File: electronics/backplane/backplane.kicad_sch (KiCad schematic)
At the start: 22 parts, among them J1 USB_C_SOCKET_RA_PTH_SIMPLE, P1 JST_SH_4_RA, P2 JST_SH_4_RA, P3 JST_SH_4_RA, P4 JST_SH_4_RA, P5 PAD_SOLDER_2mm, SW1 B3U-1000P_SPST-NO_SMD, SW2 B3U-1000P_SPST-NO_SMD, U1 USBLC6, X1 MICROMOD_PROCESSOR_SOCKET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

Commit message: Backplane schematic capture and PCB shape
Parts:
- removed F1: 0.5A_1210L_PTC, Applidyne_Fuse:FUSC3225X85L50N, symbol appli_fuse:0.5A_1210L_PTC
- removed J1: USB_C_SOCKET_RA_PTH_SIMPLE, Applidyne_USB:USB_C_PTH_GCT_USB4085, symbol appli_usb:USB_C_SOCKET_RA_PTH_SIMPLE
- removed MNT1, MNT2, MNT3: M2.5_SMD_2.5MM_THREADED, Applidyne_Mount:9774025151R, symbol appli_mount:M2.5_SMD_2.5MM_THREADED
- removed P1, P2, P3, P4: JST_SH_4_RA, Applidyne_Connector_JST:SM04B-SRSS-TB, symbol appli_connector_jst:JST_SH_4_RA
- removed P5: PAD_SOLDER_2mm, Applidyne_Connector:PAD_SOLDER_2mm, symbol appli_connector:PAD_SOLDER_2mm
- removed R1, R2, R3, R4: 4K7_1608M, Applidyne_Resistor:RESC1608X50N, symbol appli_resistor:4K7_1608M
- removed R5, R6: 4K99_1608M, Applidyne_Resistor:RESC1608X50N, symbol appli_resistor:4K99_1608M
- removed SW1, SW2: B3U-1000P_SPST-NO_SMD, Applidyne_Switch:B3U-1000P, symbol appli_switch:B3U-1000P_SPST-NO_SMD
- removed U1: USBLC6, Applidyne_SOT:SOT95P280X145-6L50N, symbol appli_device:USBLC6
- removed X1: MICROMOD_PROCESSOR_SOCKET, Applidyne_Connector_TE_Connectivity:TE_2199230-4, symbol appli_connector:M2_SMT_SOCKET_MICROMOD
- removed X2: SWD_SMT_SOCKET, Applidyne_Connector:CNCTECH_3220-10-0300-00, symbol appli_connector:SWD_SMT_SOCKET
- removed X3: MICROMOD_FUNCTION_BOARD_SOCKET, Applidyne_Connector_TE_Connectivity:TE_2199230-4, symbol appli_connector:M2_SMT_SOCKET_MICROMOD_FN
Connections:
- no-connect marks 4 -> 0
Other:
- added sheet Expansion IO (expansion.kicad_sch)
- added sheet Function Board (function-board.kicad_sch)
- added sheet Power Regulation (power.kicad_sch)
- added sheet Processor (processor.kicad_sch)
- added sheet USB Input (usb-input.kicad_sch)
- added sheet onboard-lighting (lighting.kicad_sch)
- note removed: "5k1 requests 5V@1.5A"
- note removed: "BACKPLANE"
- note removed: "I2C BUS 0"
- note removed: "I2C BUS 1"
- note removed: "MicroMod Function Board"
- note removed: "Processor board is responsible for pull resistors or circuitry."
- note removed: "QWIIC HEADERS"
- note removed: "RESET/BOOT BUTTONS"
- note removed: "SWD DEBUG"
- note removed: "USBC"

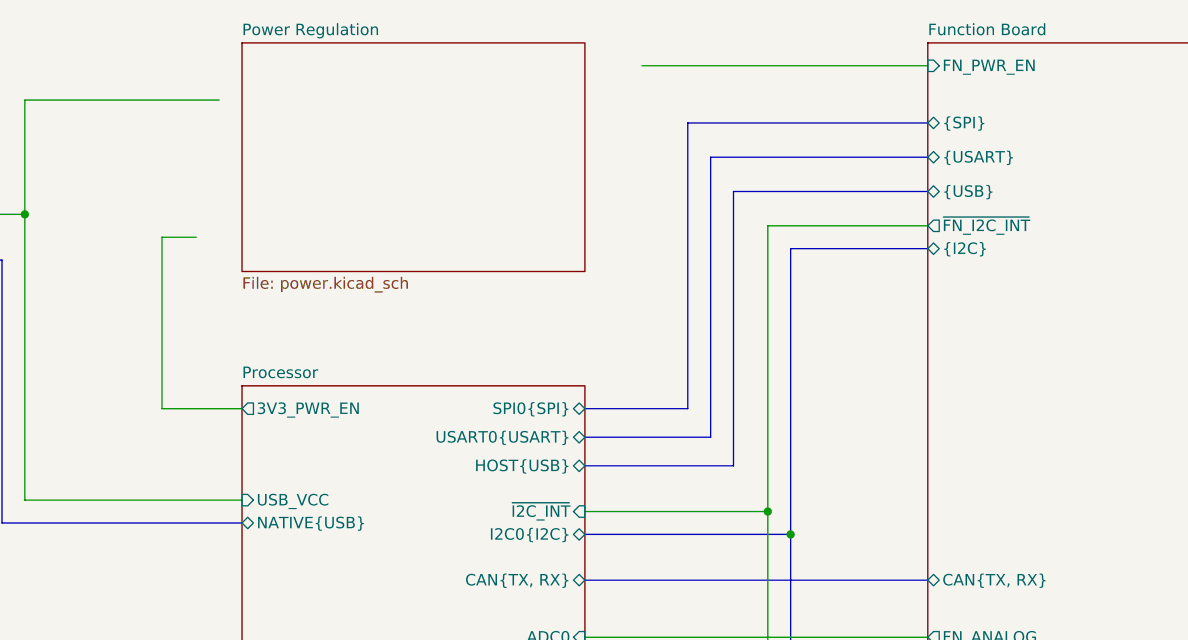
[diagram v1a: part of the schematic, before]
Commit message: Continue backplane PCB
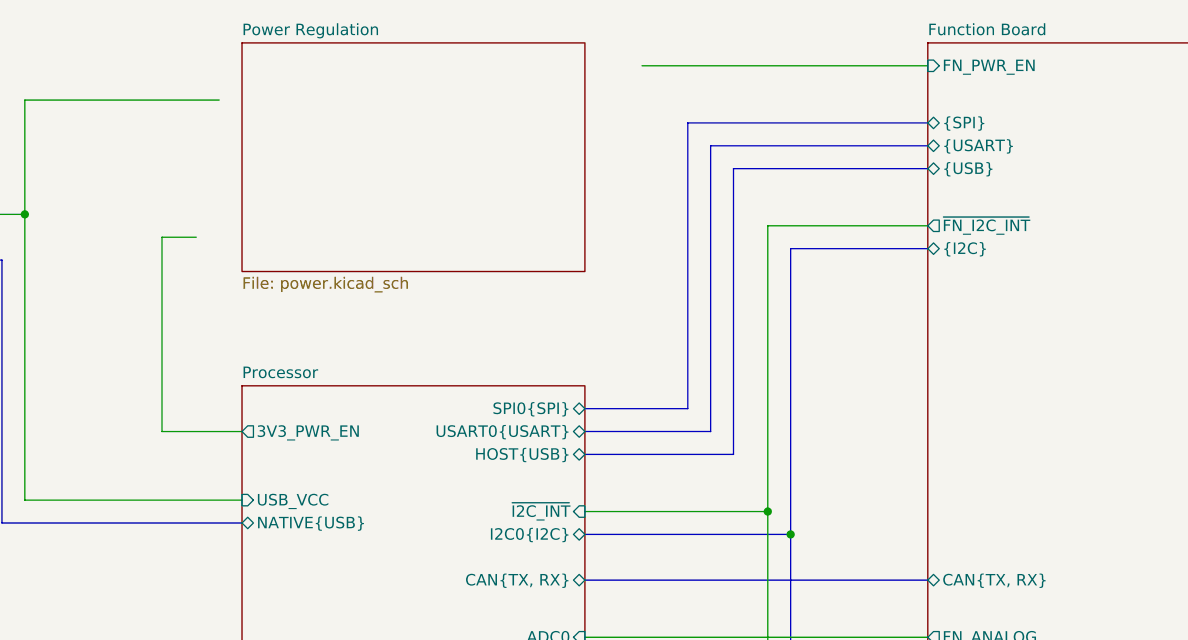
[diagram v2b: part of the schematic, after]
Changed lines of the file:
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@@
     (stroke (width 0) (type default))
   )
-  (bus (pts (xy 168.91 72.39) (xy 168.91 41.91))
+  (bus (pts (xy 168.91 71.12) (xy 168.91 39.37))
     (stroke (width 0) (type default))
   )
@@
     (stroke (width 0) (type default))
   )
-  (wire (pts (xy 105.41 66.04) (xy 105.41 46.99))
+  (wire (pts (xy 105.41 68.58) (xy 105.41 46.99))
     (stroke (width 0) (type default))
   )
-  (wire (pts (xy 114.3 66.04) (xy 105.41 66.04))
+  (wire (pts (xy 114.3 68.58) (xy 105.41 68.58))
     (stroke (width 0) (type default))
   )
@@
     (stroke (width 0) (type default))
   )
-  (bus (pts (xy 166.37 69.215) (xy 166.37 38.1))
+  (bus (pts (xy 166.37 68.58) (xy 166.37 36.83))
     (stroke (width 0) (type default))
   )
@@
     (stroke (width 0) (type default))
   )
-  (bus (pts (xy 152.4 72.39) (xy 168.91 72.39))
+  (bus (pts (xy 152.4 71.12) (xy 168.91 71.12))
     (stroke (width 0) (type default))
   )
@@
     (stroke (width 0) (type default))
   )
-  (bus (pts (xy 166.37 38.1) (xy 190.5 38.1))
+  (bus (pts (xy 166.37 36.83) (xy 190.5 36.83))
     (stroke (width 0) (type default))
   )
-  (bus (pts (xy 152.4 69.215) (xy 166.37 69.215))
+  (bus (pts (xy 152.4 68.58) (xy 166.37 68.58))
     (stroke (width 0) (type default))
   )
-  (bus (pts (xy 168.91 41.91) (xy 190.5 41.91))
+  (bus (pts (xy 168.91 39.37) (xy 190.5 39.37))
     (stroke (width 0) (type default))
   )
@@
       (effects (font (size 1.27 1.27)) (justify right))
     )
-    (pin "USART0{USART}" bidirectional (at 152.4 69.215 0)
+    (pin "USART0{USART}" bidirectional (at 152.4 68.58 0)
       (effects (font (size 1.27 1.27)) (justify right))
     )
@@
       (effects (font (size 1.27 1.27)) (justify right))
     )
-    (pin "3V3_PWR_EN" output (at 114.3 66.04 180)
+    (pin "3V3_PWR_EN" output (at 114.3 68.58 180)
       (effects (font (size 1.27 1.27)) (justify left))
     )
@@
       (effects (font (size 1.27 1.27)) (justify left))
     )
-    (pin "HOST{USB}" bidirectional (at 152.4 72.39 0)
+    (pin "HOST{USB}" bidirectional (at 152.4 71.12 0)
       (effects (font (size 1.27 1.27)) (justify right))
     )
@@
       (effects (font (size 1.27 1.27)) (justify left))
     )
-    (pin "{USART}" bidirectional (at 190.5 38.1 180)
+    (pin "{USART}" bidirectional (at 190.5 36.83 180)
       (effects (font (size 1.27 1.27)) (justify left))
     )
@@
       (effects (font (size 1.27 1.27)) (justify left))
     )
-    (pin "{USB}" bidirectional (at 190.5 41.91 180)
+    (pin "{USB}" bidirectional (at 190.5 39.37 180)
       (effects (font (size 1.27 1.27)) (justify left))
     )

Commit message: Continue backplane
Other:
- removed sheet onboard-lighting
- sheet Expansion IO ports: added PWM_OUTPUT, {UART}; removed none
- sheet Power Regulation ports: added USB_VCC; removed none
- sheet Processor ports: added FN_PWR_EN, G[5..9]; removed none
- note added: "General findings after diving into MicroMod ecosystem for this design! ESP32, STM32, SAMD51, RP2040 don't connect (or oversubscribe) TX2. ESP32, SAMD51, STM32 boards don't connect SPI1. RP2040 shares G5-8 with SPI0 lines. I haven't found any boards which correctly implement: - RTC battery connection - SWO pin on designated G11 - Only STM32, SAMD51 have CAN pinout connected. RP2040 lacks second (I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"
- note added: "NOTES"
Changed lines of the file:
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@@
+    (stroke (width 0) (type default))
+  )
+  (wire (pts (xy 158.75 27.94) (xy 158.75 57.15))
     (stroke (width 0) (type default))
   )
@@
     (stroke (width 0) (type default))
   )
+  (wire (pts (xy 107.95 57.15) (xy 158.75 57.15))
+    (stroke (width 0) (type default))
+  )
   (bus (pts (xy 87.63 78.74) (xy 114.3 78.74))
     (stroke (width 0) (type default))
@@
     (stroke (width 0) (type default))
   )
-  (wire (pts (xy 90.17 44.45) (xy 90.17 31.75))
+  (wire (pts (xy 90.17 34.29) (xy 90.17 44.45))
     (stroke (width 0) (type default))
   )
@@
     (stroke (width 0) (type default))
   )
-  (wire (pts (xy 105.41 68.58) (xy 105.41 46.99))
-    (stroke (width 0) (type default))
-  )
-  (wire (pts (xy 114.3 68.58) (xy 105.41 68.58))
+  (wire (pts (xy 90.17 34.29) (xy 114.3 34.29))
+    (stroke (width 0) (type default))
+  )
+  (bus (pts (xy 152.4 124.46) (xy 190.5 124.46))
     (stroke (width 0) (type default))
   )
@@
     (stroke (width 0) (type default))
   )
-  (wire (pts (xy 105.41 46.99) (xy 109.22 46.99))
-    (stroke (width 0) (type default))
-  )
   (wire (pts (xy 90.17 76.2) (xy 114.3 76.2))
     (stroke (width 0) (type default))
@@
     (stroke (width 0) (type default))
   )
-  (wire (pts (xy 90.17 31.75) (xy 111.76 31.75))
-    (stroke (width 0) (type default))
-  )
   (bus (pts (xy 190.5 115.57) (xy 175.26 115.57))
     (stroke (width 0) (type default))
@@
     (stroke (width 0) (type default))
   )
+  (wire (pts (xy 114.3 66.04) (xy 107.95 66.04))
+    (stroke (width 0) (type default))
+  )
+  (wire (pts (xy 107.95 66.04) (xy 107.95 57.15))
+    (stroke (width 0) (type default))
+  )
   (bus (pts (xy 175.26 48.26) (xy 190.5 48.26))
     (stroke (width 0) (type default))
@@
     (stroke (width 0) (type default))
   )
+  (text "NOTES" (at 33.02 160.02 0)
+    (effects (font (size 2 2) (thickness 0.4) bold) (justify left bottom))
+  )
+  (text "General findings after diving into MicroMod ecosystem for this design!\n\nESP32, STM32, SAMD51, RP2040 don't connect (or oversubscribe) TX2.\nESP32, SAMD51, STM32 boards don't connect SPI1.\nRP2040 shares G5-8 with SPI0 lines.\n\nI haven't found any boards which correctly implement:\n- RTC battery connection\n- SWO pin on designated G11\n- \n\nOnly STM32, SAMD51 have CAN pinout connected.\n\nRP2040 lacks second (I2C1) bus connections.\n"
+    (at 13.97 195.58 0)
+    (effects (font (size 1.27 1.27)) (justify left bottom))
+  )
   (sheet (at 114.3 63.5) (size 38.1 76.2) (fields_autoplaced)
     (stroke (width 0.1524) (type solid))
@@
       (effects (font (size 1.27 1.27)) (justify right))
     )
+    (pin "FN_PWR_EN" output (at 114.3 66.04 180)
+      (effects (font (size 1.27 1.27)) (justify left))
+    )
+    (pin "G[5..9]" bidirectional (at 152.4 115.57 0)
+      (effects (font (size 1.27 1.27)) (justify right))
+    )
     (instances
       (project "backplane"
@@
       (effects (font (size 1.27 1.27)) (justify left))
     )
+    (pin "{UART}" bidirectional (at 190.5 124.46 180)
+      (effects (font (size 1.27 1.27)) (justify left))
+    )
+    (pin "PWM_OUTPUT" bidirectional (at 190.5 133.35 180)
+      (effects (font (size 1.27 1.27)) (justify left))
+    )
     (instances
       (project "backplane"
@@
       (effects (font (size 1.27 1.27)) (justify left top))
     )
+    (pin "USB_VCC" input (at 114.3 34.29 180)
+      (effects (font (size 1.27 1.27)) (justify left))
+    )
     (instances
       (project "backplane"
@@
       )
     )
-  )
-  (sheet (at 38.1 127) (size 38.1 12.7) (fields_autoplaced)
-    (stroke (width 0.1524) (type solid))
-    (fill (color 0 0 0 0.0000))
-    (property "Sheetname" "onboard-lighting" (at 38.1 126.2884 0)
-      (effects (font (size 1.27 1.27)) (justify left bottom))
-    )
-    (property "Sheetfile" "lighting.kicad_sch" (at 38.1 140.2846 0)
-      (effects (font (size 1.27 1.27)) (justify left top))
-    )
-    (instances
-      (project "backplane"
-        (path "/0bfdf1e4-b99d-46d4-adfc-42d352d37946" (page "6"))
-      )
-    )

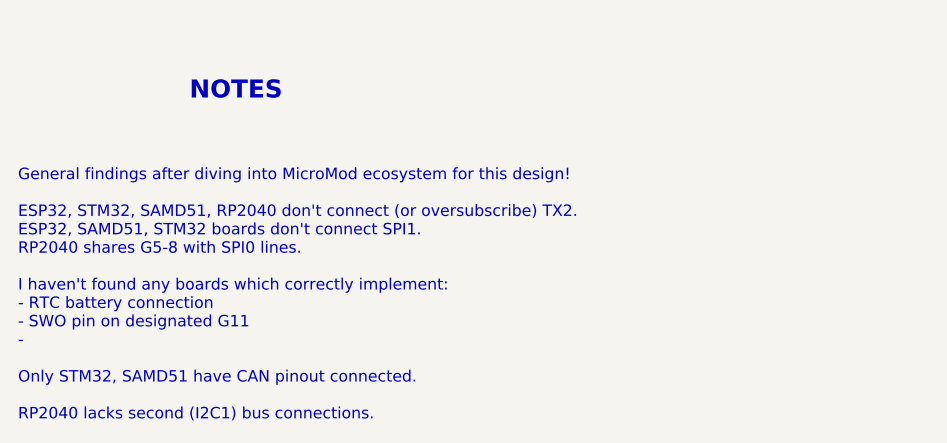
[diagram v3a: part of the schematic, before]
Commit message: Continue schematic tweaks, start routing backplane
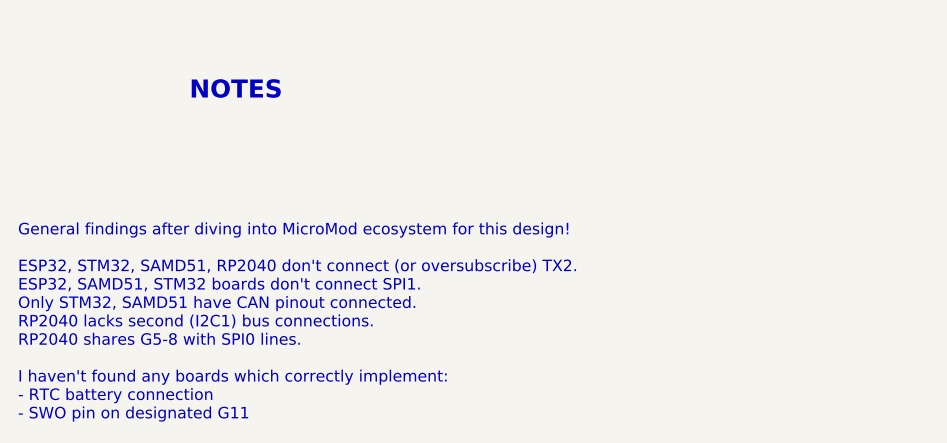
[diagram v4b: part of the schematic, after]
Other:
- note added: "General findings after diving into MicroMod ecosystem for this design! ESP32, STM32, SAMD51, RP2040 don't connect (or oversubscribe) TX2. ESP32, SAMD51, STM32 boards don't connect SPI1. Only STM32, SAMD51 have CAN pinout connected. RP2040 lacks second (I2C1) bus connections. RP2040 shares G5-8 with SPI0 lines. I haven't found any boards which correctly implement: - RTC battery connection - SWO pi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"
- note removed: "General findings after diving into MicroMod ecosystem for this design! ESP32, STM32, SAMD51, RP2040 don't connect (or oversubscribe) TX2. ESP32, SAMD51, STM32 boards don't connect SPI1. RP2040 shares G5-8 with SPI0 lines. I haven't found any boards which correctly implement: - RTC battery connection - SWO pin on designated G11 - Only STM32, SAMD51 have CAN pinout connected. RP2040 lacks second (I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"
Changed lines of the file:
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@@
     (effects (font (size 2 2) (thickness 0.4) bold) (justify left bottom))
   )
-  (text "General findings after diving into MicroMod ecosystem for this design!\n\nESP32, STM32, SAMD51, RP2040 don't connect (or oversubscribe) TX2.\nESP32, SAMD51, STM32 boards don't connect SPI1.\nRP2040 shares G5-8 with SPI0 lines.\n\nI haven't found any boards which correctly implement:\n- RTC battery connection\n- SWO pin on designated G11\n- \n\nOnly STM32, SAMD51 have CAN pinout connected.\n\nRP2040 lacks second (I2C1) bus connections.\n"
+  (text "General findings after diving into MicroMod ecosystem for this design!\n\nESP32, STM32, SAMD51, RP2040 don't connect (or oversubscribe) TX2.\nESP32, SAMD51, STM32 boards don't connect SPI1.\nOnly STM32, SAMD51 have CAN pinout connected.\nRP2040 lacks second (I2C1) bus connections.\nRP2040 shares G5-8 with SPI0 lines.\n\nI haven't found any boards which correctly implement:\n- RTC battery connection\n- SWO pin on designated G11"
     (at 13.97 195.58 0)
     (effects (font (size 1.27 1.27)) (justify left bottom))
